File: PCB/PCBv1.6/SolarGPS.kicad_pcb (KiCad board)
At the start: 2 copper layers, 80 x 30 mm, 46 parts, among them J1 Conn_01x10_Female, J2 Solar2+, J3 Solar1+, J4 GND, J5 GND, J6 Conn_02x03_Odd_Even, J7 Screw_Terminal_01x01, J8 Conn_01x04_Male, U1 BQ25505, U2 MAX-M10Q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

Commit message: More Progress
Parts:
- removed D2: LED, Diode_SMD:D_0805_2012Metric
- removed R2, R3: 100, Resistor_SMD:R_0603_1608Metric
- U2: value MAX-M10Q -> MAX-M10S; footprint RF_GPS:ublox_MAX -> Margo_Lib:MAX-8
- moved U2 6.90 mm to (119.5, 77.1)
- moved R4 4.80 mm to (70.2, 75.8)
- moved J7 1.00 mm to (53.0, 65.0)
- moved C1 0.16 mm to (128.5, 65.8)
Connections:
- net SOLAR+ renamed /SOLAR+
- J1 pad 5: DISPEN -> VBAT_OK
- U2 pad 6: GPS_VDD -> VDD
- U3 pad 10: Net-(U3-Pad10) -> GPS_EN
- U3 pad 18: DISPEN -> unconnected-(U3-Pad18)
- U3 pad 19: LED -> unconnected-(U3-Pad19)
- U3 pad 24: GPS_EN -> unconnected-(U3-Pad24)
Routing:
- net /SOLAR+: track 32.1 -> 11.7 mm, vias 2 -> 0
- net VDD: track 154.1 -> 174.6 mm, vias 8 -> 10
- net LED: track 18.3 -> 0.00 mm, vias 2 -> 0
- net DISPEN: track 13.7 -> 0.00 mm, vias 2 -> 0
- net GPS_EN: track 65.8 -> 56.4 mm, vias 2 -> 0
- net Net-(U3-Pad10): track 6.18 -> 0.00 mm
- net Net-(D2-Pad2): track 1.34 -> 0.00 mm
- net EXTCOMIN: track 25.0 -> 23.9 mm
- net GPS_VDD: track 20.6 -> 19.5 mm
- net DISPCS: track 9.71 -> 9.10 mm
- net VBAT_OK: track 37.5 -> 37.6 mm, vias 3 -> 4

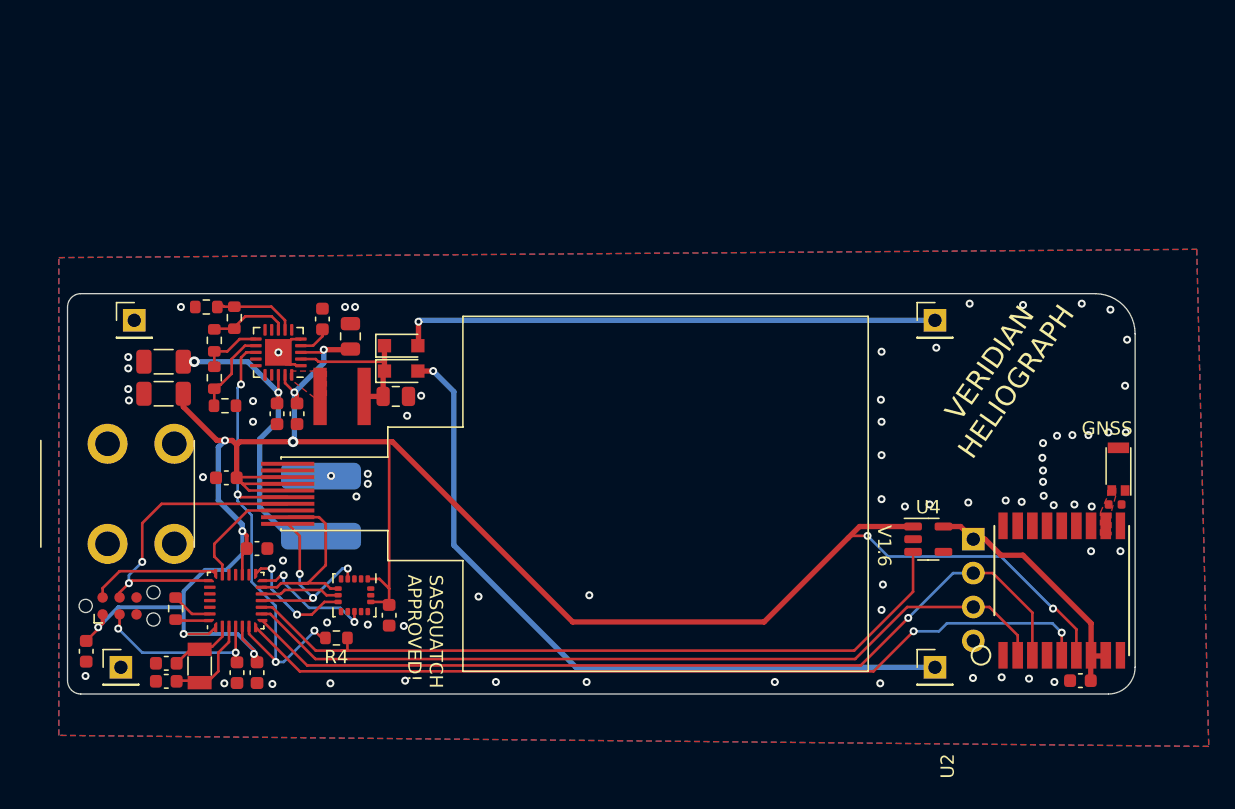
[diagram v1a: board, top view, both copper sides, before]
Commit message: Replace GNSS with L96
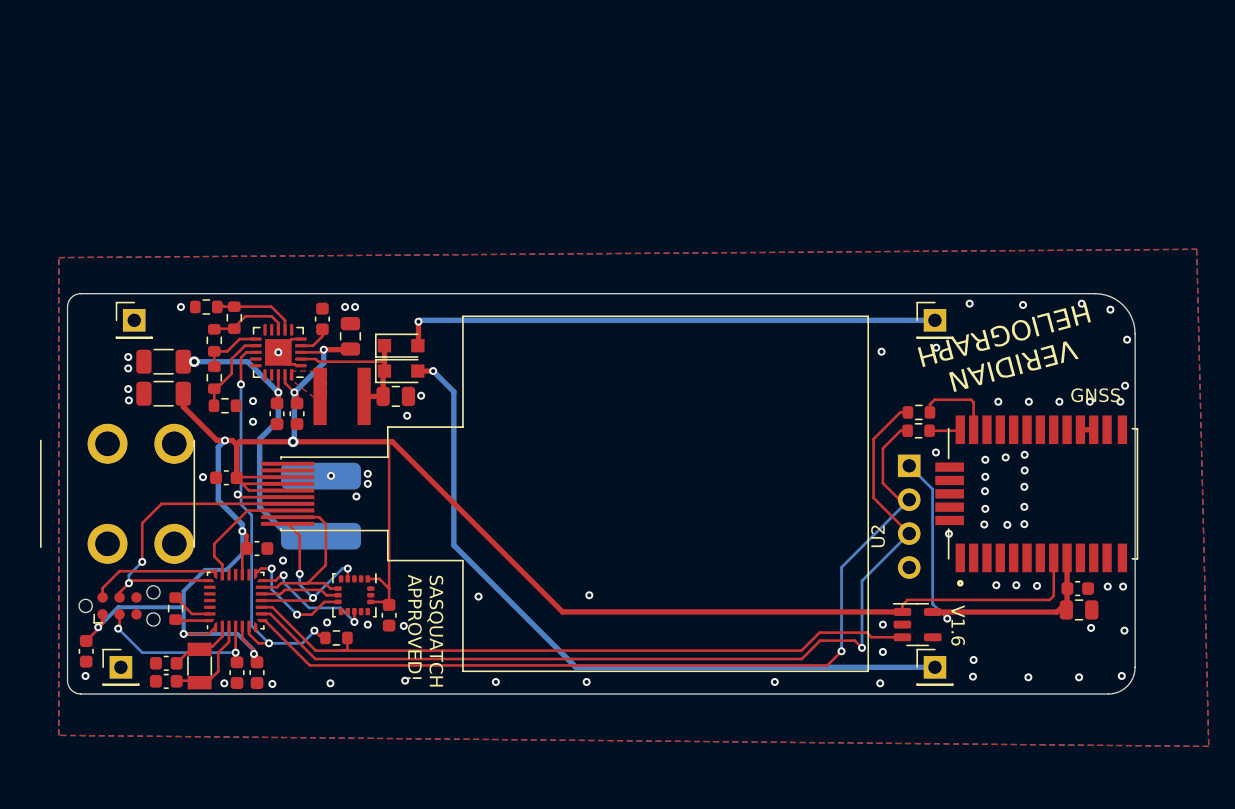
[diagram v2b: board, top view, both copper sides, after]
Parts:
- removed AE1: Antenna_Shield, RF_Antenna:Pulse_W3011
- added FB2: 1k@100MHz, Resistor_SMD:R_0603_1608Metric, F.Cu at (113.8, 60.3)
- added FB3: 1k@100MHz, Resistor_SMD:R_0603_1608Metric, F.Cu at (113.8, 58.9)
- C1: value 3.3pF -> 1uF; footprint Capacitor_SMD:C_0402_1005Metric -> Capacitor_SMD:C_0603_1608Metric
- C5: value 1uF -> 4.7uF; footprint Capacitor_SMD:C_0603_1608Metric -> Capacitor_SMD:C_0805_2012Metric
- U2: value MAX-M10S -> L96-M33; footprint Margo_Lib:MAX-8 -> Heliograph:XCVR_L96-M33
- moved U2 12.6 mm to (123.1, 65.0)
- moved J8 7.30 mm to (113.1, 62.9)
- moved C1 6.89 mm to (125.7, 72.1)
- moved U4 6.45 mm to (113.7, 74.8)
- moved C5 5.30 mm to (125.8, 73.7), turned to 180 degrees
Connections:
- C1 pad 2: /GPS_RF -> GPS_VDD
- U2 pad 1: GND -> (no net)
- U2 pad 11: /GPS_RF -> GND
- U2 pad 13: unconnected-(U2-Pad13) -> GND
- U2 pad 14: unconnected-(U2-Pad14) -> GND
- U2 pad 15: unconnected-(U2-Pad15) -> GND
- U2 pad 16: unconnected-(U2-Pad16) -> /GPS_RF
- U2 pad 17: unconnected-(U2-Pad17) -> /GPS_RF
- U2 pad 18: unconnected-(U2-Pad18) -> GND
- U2 pad 2: GPS_UART_MISO -> unconnected-(U2-Pad2)
- U2 pad 3: GPS_UART_MOSI -> unconnected-(U2-Pad3)
- U2 pad 4: unconnected-(U2-Pad4) -> GND
- U2 pad 5: GPS_EXINT -> GND
- U2 pad 6: VDD -> unconnected-(U2-Pad6)
- U2 pad 7: GPS_VDD -> unconnected-(U2-Pad7)
- U2 pad 8: GPS_VDD -> VDD
- U2 pad 9: unconnected-(U2-Pad9) -> GPS_VDD
- U3 pad 7: GPS_EXINT -> unconnected-(U3-Pad7)
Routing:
- net GPS_EXINT: track 65.3 -> 0.00 mm, vias 2 -> 0
- net VDD: track 174.6 -> 163.7 mm, vias 10 -> 8
- net GPS_VDD: track 19.5 -> 27.6 mm, vias 0 -> 1
- net GPS_UART_MISO: track 62.1 -> 68.8 mm, vias 0 -> 1
- net Net-(U2-Pad25): track 0.00 -> 6.15 mm
- net GPS_EN: track 56.4 -> 51.5 mm
- net VBAT_OK: track 37.6 -> 34.6 mm
- net Net-(U2-Pad26): track 0.00 -> 2.33 mm
- net /GPS_RF: track 0.00 -> 1.00 mm
- net GND: vias 70 -> 73
- removed copper zone on F.Cu, net /GPS_RF

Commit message: Update PCBV10
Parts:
- removed C11: 4.7uF, Capacitor_SMD:C_0805_2012Metric
- removed C12: 47uF, Capacitor_SMD:C_1206_3216Metric
- removed D3: Schottky, Diode_SMD:D_SOD-323_HandSoldering
- removed ROK1, ROV1, ROV2: 6.49M, Resistor_SMD:R_0603_1608Metric
- removed ROK2: 5.36M, Resistor_SMD:R_0603_1608Metric
- removed ROK3: 1M, Resistor_SMD:R_0603_1608Metric
- added D2: Schottky, Diode_SMD:D_SOD-323_HandSoldering, F.Cu at (77.1, 52.7)
- added R2: 1M, Resistor_SMD:R_0603_1608Metric, F.Cu at (66.4, 53.0)
- added R3: 1M, Resistor_SMD:R_0603_1608Metric, F.Cu at (63.5, 53.0)
- added R6: 432k, Resistor_SMD:R_0603_1608Metric, F.Cu at (63.8, 57.2)
- added R7: 86k, Resistor_SMD:R_0603_1608Metric, F.Cu at (63.8, 55.9)
- C4: value 4.7uF -> 25F; footprint Capacitor_SMD:C_0805_2012Metric -> Heliograph:TPLC3R8-25MR8X20; moved to B.Cu
- C6: value 10nF -> 1uF
- C7: value 10nF -> 0.1uF
- C8: value 25F -> 10nF; footprint Heliograph:TPLC3R8-25MR8X20 -> Capacitor_SMD:C_0603_1608Metric; moved to F.Cu
- C9: value 10nF -> 47uF; footprint Capacitor_SMD:C_0603_1608Metric -> Capacitor_SMD:C_1206_3216Metric
- J2: value Solar2+ -> GND
- J3: value Solar1+ -> GND
- J4: value GND -> Solar1+
- J5: value GND -> Solar2+
- L1: value 22uH -> 0.47uH; footprint Heliograph:744031220 -> Inductor_SMD:L_0805_2012Metric_Pad1.05x1.20mm_HandSolder
- U1: value BQ25505 -> TPS63802; footprint Package_DFN_QFN:QFN-20-1EP_3.5x3.5mm_P0.5mm_EP2x2mm -> Margo_Lib:VREG_TPS63802DLAR
- moved J5 58.3 mm to (91.5, 33.4)
- moved J3 50.8 mm to (85.5, 36.7)
- moved J2 37.5 mm to (80.8, 36.7)
- moved J4 23.4 mm to (73.8, 38.0)
- moved C10 16.6 mm to (73.7, 53.4), turned to 90 degrees
- moved C8 9.37 mm to (68.1, 57.6)
- moved C7 8.19 mm to (63.5, 51.7), turned to 0 degrees
- moved C4 7.59 mm to (75.4, 65.2)
- moved L1 3.37 mm to (70.4, 55.2), turned to -90 degrees
- moved U1 2.49 mm to (68.1, 55.4), turned to 0 degrees
- moved D1 2.25 mm to (77.1, 54.6)
- moved C9 2.06 mm to (67.7, 59.5), turned to 0 degrees
- moved C6 0.46 mm to (68.9, 52.3), turned to -90 degrees
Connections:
- C10 pad 2: VBAT -> /VBAT
- C4 pad 1: /SOLAR+ -> /VBAT
- C6 pad 1: Net-(C6-Pad1) -> GND
- C6 pad 2: GND -> /VBAT
- C7 pad 2: VDD -> VBATSENSE
- C8 pad 1: VBAT -> GND
- C8 pad 2: GND -> VDD
- C9 pad 2: VBAT -> VDD
- D1 pad 1: /SOLAR+ -> /VBAT
- D1 pad 2: Net-(D1-Pad2) -> /SOLAR1+
- J1 pad 5: VBAT_OK -> VDD
- J2 pad 1: Net-(D1-Pad2) -> GND
- J3 pad 1: Net-(D3-Pad2) -> GND
- J4 pad 1: GND -> /SOLAR1+
- J5 pad 1: GND -> /SOLAR2+
- L1 pad 1: /SOLAR+ -> Net-(U1-Pad9)
- L1 pad 2: /LBOOST -> Net-(U1-Pad7)
- R4 pad 2: VBAT_OK -> GND
- U1 pad 1: GND -> VBATSENSE
- U1 pad 10: unconnected-(U1-Pad10) -> /VBAT
- U1 pad 2: /SOLAR+ -> GND
- U1 pad 3: VDD -> GND
- U1 pad 4: Net-(C6-Pad1) -> /FB
- U1 pad 5: GND -> unconnected-(U1-Pad5)
- U1 pad 6: unconnected-(U1-Pad6) -> VDD
- U1 pad 7: Net-(ROV1-Pad1) -> Net-(U1-Pad7)
- U1 pad 8: /VRDIV -> GND
- U1 pad 9: unconnected-(U1-Pad9) -> Net-(U1-Pad9)
- U3 pad 6: VBAT_OK -> unconnected-(U3-Pad6)
- U3 pad 7: unconnected-(U3-Pad7) -> VBATSENSE
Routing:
- net Net-(D3-Pad2): track 54.7 -> 0.00 mm, vias 1 -> 0
- net Net-(D1-Pad2): track 40.6 -> 0.00 mm, vias 1 -> 0
- net VBAT_OK: track 34.6 -> 0.00 mm, vias 4 -> 0
- net VBATSENSE: track 0.00 -> 30.8 mm, vias 0 -> 2
- net /VBAT: track 0.00 -> 30.1 mm, vias 0 -> 1
- net VBAT: track 24.9 -> 0.00 mm, vias 2 -> 0
- net /SOLAR+: track 11.7 -> 0.00 mm
- net VDD: track 163.7 -> 156.2 mm, vias 8 -> 5
- net Net-(ROV1-Pad1): track 6.13 -> 0.00 mm
- net Net-(ROK1-Pad1): track 5.95 -> 0.00 mm
- net /VRDIV: track 5.92 -> 0.00 mm
- net Net-(ROK2-Pad1): track 4.65 -> 0.00 mm
- net /FB: track 0.00 -> 3.92 mm
- net Net-(C6-Pad1): track 2.43 -> 0.00 mm
- net Net-(U1-Pad9): track 0.00 -> 1.90 mm
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- removed copper zone on F.Cu, net /LBOOST

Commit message: PCB1.6
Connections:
- J1 pad 4: EXTCOMIN -> unconnected-(J1-Pad4)
- J1 pad 5: VDD -> LCDEN
- J1 pad 8: VDD -> GND
- J6 pad 4: EXTCOMIN -> SWCLK
- U3 pad 19: unconnected-(U3-Pad19) -> DISPCS
- U3 pad 20: DISPCS -> LCDEN
- U3 pad 22: EXTCOMIN -> SWCLK
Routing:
- net EXTCOMIN: track 23.9 -> 0.00 mm, vias 2 -> 0
- net LCDEN: track 0.00 -> 9.66 mm
- net SWCLK: track 0.00 -> 7.44 mm
- net VDD: track 156.2 -> 149.3 mm
- net DISPCS: track 9.10 -> 8.48 mm
